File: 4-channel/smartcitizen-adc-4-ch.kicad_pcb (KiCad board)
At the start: 2 copper layers, 37.2 x 49.7 mm, 31 parts, among them J1 EXT-V, J2 EXT-V, M1 PINHD-1x10-HEADER, T1 NMOSFET, T2 NMOSFET, U1 ADS1115IDGS

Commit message: 4-channel exports
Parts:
- removed EXT-V1, EXT-V2: PINHD-1x02-HEADER, fab:fab-1X02
- removed G***: LOGO, LOGO:Logo_5000
- removed I2, I3: alphasense-isb, ALPHASENSE:alphasense-isb
- added M2: PINHD-2X2-SMD, fab-2X02SMD, F.Cu at (142.5, 102.2)
- R1, R2, R3, R4, R5, R6: footprint fab:fab-R1206FAB -> fab-R1206FAB
- T1, T2: footprint fab:fab-SOT-23 -> fab-SOT-23
- moved ISB_1 48.0 mm to (156.0, 62.3)
- moved J1 11.7 mm to (142.5, 66.3)
- moved J2 11.7 mm to (169.6, 69.8)
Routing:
- net 5V: track 64.2 -> 84.6 mm
- net VCC: track 93.5 -> 109.8 mm, vias 2 -> 1
- net GND: track 166.5 -> 182.4 mm
- net A3: track 31.5 -> 25.0 mm, vias 0 -> 1
- net A0: track 40.1 -> 42.7 mm
- net A1: track 37.4 -> 35.0 mm, vias 1 -> 2
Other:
- board size 37.2 x 49.7 mm -> 37.3 x 58.1 mm
- board text added: "06/07/2020"
- board text removed: "29/06/2020"

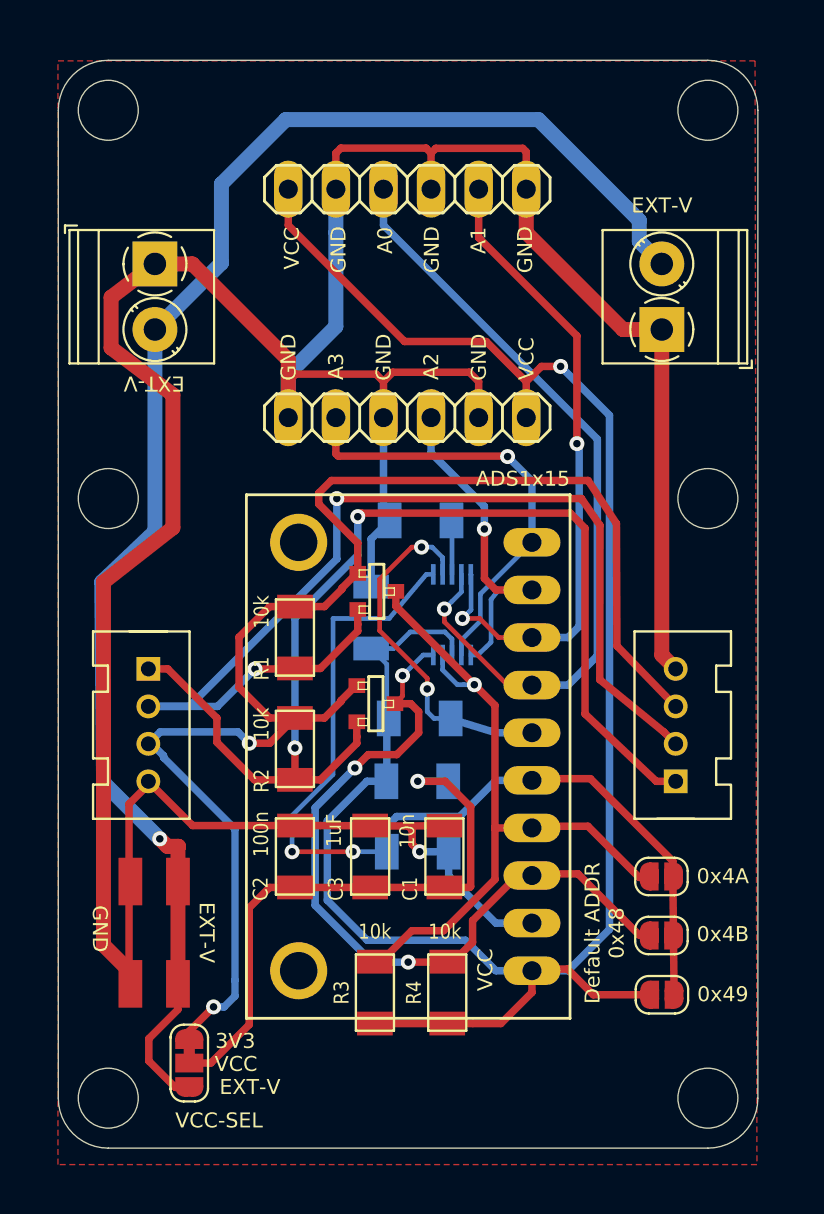
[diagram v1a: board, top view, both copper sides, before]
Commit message: 4-channel on pcb version
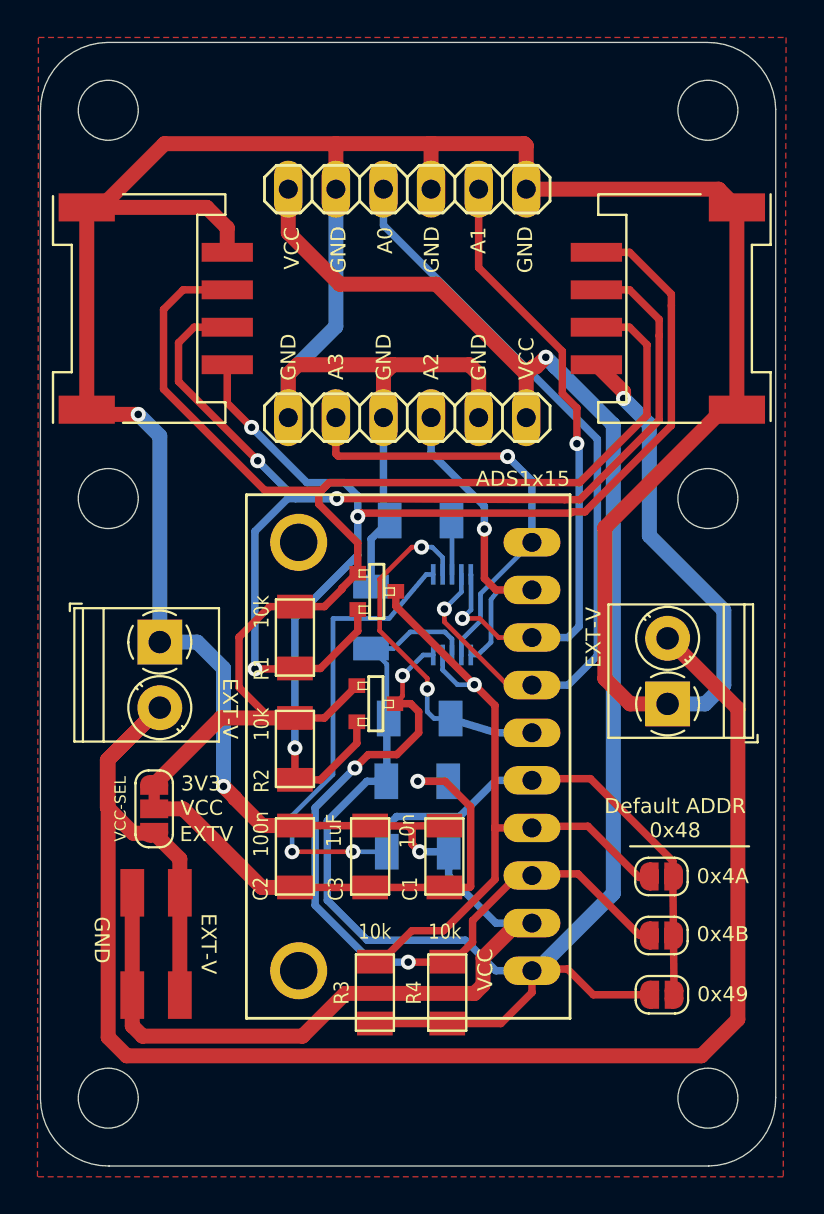
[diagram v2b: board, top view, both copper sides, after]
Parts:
- added G***: LOGO, LOGO:Logo_5000, B.Cu at (148.5, 109.4)
- GROVEIN1: value GROVE-CONNECTOR-DIP_4P-2.0_ -> GROVE-CONNECTOR-SMD-90D_4+2P-2.0_; footprint OPL_Connector:HW4-2.0 -> OPL_Connector:HW4-SMD-2.0-90D
- GROVEOUT1: footprint OPL_Connector:HW4-2.0 -> OPL_Connector:HW4-SMD-2.0-90D
- moved GROVEIN1 36.3 mm to (141.6, 68.7)
- moved GROVEOUT1 36.3 mm to (170.9, 68.7)
- moved J1 20.2 mm to (142.8, 86.5)
- moved J2 20.0 mm to (169.9, 89.8)
- moved JP1 13.7 mm to (142.5, 95.4)
- moved M2 0.61 mm to (142.6, 102.8)
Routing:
- net GND: track 182.4 -> 243.9 mm, vias 1 -> 4
- net 5V: track 84.6 -> 94.2 mm, vias 1 -> 0
- net SDA3V3: track 58.9 -> 64.3 mm, vias 2 -> 3
- net Net-(C1-Pad1): track 31.8 -> 27.9 mm
- net SCL3V3: track 60.5 -> 63.7 mm, vias 2 -> 3
- net 3V3: track 79.6 -> 77.7 mm, vias 2 -> 0
- net VCC: track 109.8 -> 111.4 mm
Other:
- board size 37.3 x 58.1 mm -> 39.2 x 60 mm
- board text added: "EXTV"

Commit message: Move traces out of screw, move components to bottom layer for SMD
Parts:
- R1, R2, R3, R4, T1, T2: moved to B.Cu
- moved T2 14.8 mm to (145.2, 101.4), turned to 180 degrees
- moved T1 10.1 mm to (145.2, 79.7), turned to 180 degrees
- moved G*** 1.74 mm to (149.3, 111.0)
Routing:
- net 5V: track 94.2 -> 68.8 mm, vias 0 -> 2
- net SDA: track 40.1 -> 64.4 mm, vias 1 -> 2
- net SCL: track 41.8 -> 56.4 mm
- net 3V3: track 77.7 -> 84.9 mm, vias 0 -> 4
- net SCL3V3: track 63.7 -> 68.7 mm, vias 3 -> 2
- net SDA3V3: track 64.3 -> 61.6 mm, vias 3 -> 2
- net ALRT: track 19.2 -> 17.1 mm
- net ADDR: track 51.5 -> 50.7 mm
- net VCC: track 111.4 -> 110.7 mm
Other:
- board text added: "02/12/2020-SMD"
- board text removed: "06/07/2020"
- board text removed: "EXT-V"
